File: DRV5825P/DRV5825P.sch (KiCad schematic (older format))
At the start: 39 parts

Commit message: pcb design
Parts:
- added H1, H2, H3, H4: 3mm, MountingHole:MountingHole_3.2mm_M3_Pad, symbol Mechanical:MountingHole
- C1, C19, C20, C21, C22, C3: renamed from C?; footprint (none) -> Capacitor_SMD:C_0805_2012Metric
- C10, C11, C12, C15, C16, C17, C18, C2, C5, C7, C8, C9: renamed from C?; footprint (none) -> Capacitor_SMD:C_0603_1608Metric
- C13, C6: renamed from C?; footprint (none) -> Capacitor_SMD:C_1206_3216Metric
- C14, C4: renamed from C?; footprint (none) -> Capacitor_SMD:CP_Elec_10x14.3
- D1: renamed from D?; footprint (none) -> Diode_SMD:D_SMB
- F1: renamed from F?; footprint (none) -> Fuse:Fuse_1206_3216Metric
- FB1: renamed from FB?; footprint (none) -> Inductor_SMD:L_0805_2012Metric
- J1, J3, J4: renamed from J?; footprint (none) -> Connector_Phoenix_MC:PhoenixContact_MCV_1,5_2-G-3.5_1x02_P3.50mm_Vertical
- J2: renamed from J?; footprint (none) -> Connector_IDC:IDC-Header_2x08_P2.54mm_Vertical
- R1, R2, R3, R4, R5: renamed from R?; footprint (none) -> Resistor_SMD:R_0603_1608Metric
- gave numbers to parts that had none: 5
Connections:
- net GND: now also J2.11 (Pin_11), J2.13 (Pin_13), J2.9 (Pin_9); no longer J2.1 (Pin_1), J2.3 (Pin_3), J2.5 (Pin_5)
- net VDD: now also J2.1 (Pin_1), J2.3 (Pin_3), J2.5 (Pin_5); no longer J2.11 (Pin_11), J2.13 (Pin_13), J2.9 (Pin_9)
- net at R3.2, U1.10 (GPIO1): now also J2.4 (Pin_4); no longer J2.10 (Pin_10)
- net at R2.2, U1.11 (GPIO2): now also J2.6 (Pin_6); no longer J2.12 (Pin_12)
- net at U1.12 (LRCLK): now also J2.8 (Pin_8); no longer J2.2 (Pin_2)
- net at U1.13 (SCLK): now also J2.10 (Pin_10); no longer J2.4 (Pin_4)
- net at U1.14 (SDIN): now also J2.12 (Pin_12); no longer J2.6 (Pin_6)
- net at R4.2, U1.9 (GPIO0): now also J2.2 (Pin_2); no longer J2.8 (Pin_8)
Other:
- moved on the sheet: C1

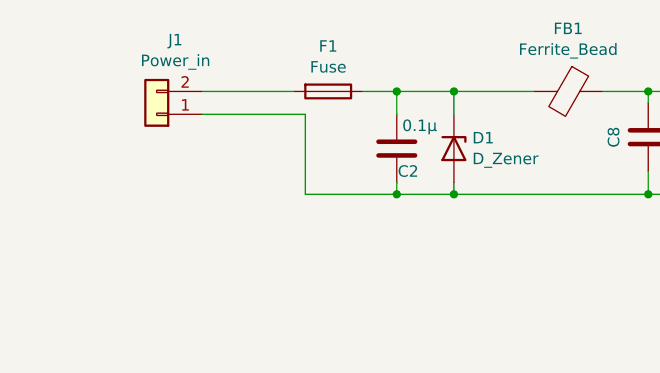
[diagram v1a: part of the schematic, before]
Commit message: teardrops added
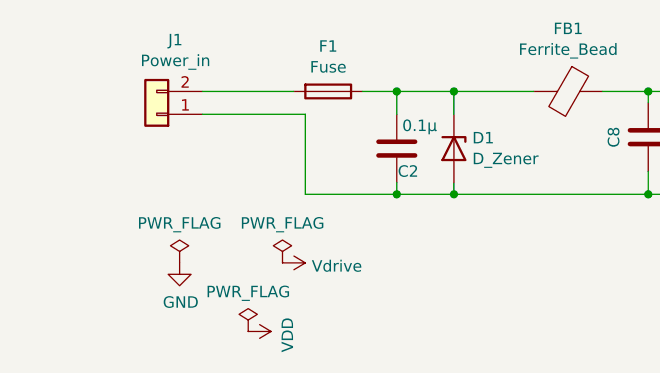
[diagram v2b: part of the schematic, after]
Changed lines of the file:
@@
 Wire Wire Line
 	1200 4450 1200 4350
+$Comp
+L power:PWR_FLAG #FLG0101
+U 1 1 60C11797
+P 1300 6850
+F 0 "#FLG0101" H 1300 6925 50  0001 C CNN
+F 1 "PWR_FLAG" H 1300 7023 50  0000 C CNN
+F 2 "" H 1300 6850 50  0001 C CNN
+F 3 "~" H 1300 6850 50  0001 C CNN
+	1    1300 6850
+	1    0    0    -1
+$EndComp
+$Comp
+L power:GND #PWR0127
+U 1 1 60C12535
+P 1300 6850
+F 0 "#PWR0127" H 1300 6600 50  0001 C CNN
+F 1 "GND" H 1305 6677 50  0000 C CNN
+F 2 "" H 1300 6850 50  0001 C CNN
+F 3 "" H 1300 6850 50  0001 C CNN
+	1    1300 6850
+	1    0    0    -1
+$EndComp
+$Comp
+L power:PWR_FLAG #FLG0102
+U 1 1 60C12875
+P 1750 6850
+F 0 "#FLG0102" H 1750 6925 50  0001 C CNN
+F 1 "PWR_FLAG" H 1750 7023 50  0000 C CNN
+F 2 "" H 1750 6850 50  0001 C CNN
+F 3 "~" H 1750 6850 50  0001 C CNN
+	1    1750 6850
+	1    0    0    -1
+$EndComp
+$Comp
+L power:Vdrive #PWR0128
+U 1 1 60C12B48
+P 1750 6850
+F 0 "#PWR0128" H 1550 6700 50  0001 C CNN
+F 1 "Vdrive" V 1765 6978 50  0000 L CNN
+F 2 "" H 1750 6850 50  0001 C CNN
+F 3 "" H 1750 6850 50  0001 C CNN
+	1    1750 6850
+	0    1    1    0
+$EndComp
+$Comp
+L power:VDD #PWR0129
+U 1 1 60C135D0
+P 1600 7150
+F 0 "#PWR0129" H 1600 7000 50  0001 C CNN
+F 1 "VDD" H 1615 7323 50  0000 C CNN
+F 2 "" H 1600 7150 50  0001 C CNN
+F 3 "" H 1600 7150 50  0001 C CNN
+	1    1600 7150
+	0    1    1    0
+$EndComp
+$Comp
+L power:PWR_FLAG #FLG0103
+U 1 1 60C14433
+P 1600 7150
+F 0 "#FLG0103" H 1600 7225 50  0001 C CNN
+F 1 "PWR_FLAG" H 1600 7323 50  0000 C CNN
+F 2 "" H 1600 7150 50  0001 C CNN
+F 3 "~" H 1600 7150 50  0001 C CNN
+	1    1600 7150
+	1    0    0    -1
+$EndComp
 $EndSCHEMATC
